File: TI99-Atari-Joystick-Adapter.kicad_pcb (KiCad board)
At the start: 2 copper layers, 13 parts, among them J1 DE9_Plug_MountingHoles, J2 DE9_Plug_MountingHoles, J3 DE9_Receptacle_MountingHoles

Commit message: Initial Design v0.01
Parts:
- added H1: MountingHole, MountingHole:MountingHole_2.5mm, F.Cu at (129.0, 59.0)
- added H2: MountingHole, MountingHole:MountingHole_2.5mm, F.Cu at (161.0, 59.0)
- added H3: MountingHole, MountingHole:MountingHole_2.5mm, F.Cu at (129.0, 132.0)
- added H4: MountingHole, MountingHole:MountingHole_2.5mm, F.Cu at (161.0, 132.0)
- D1, D10, D2, D3, D4, D5, D6, D7, D8, D9: value 1N4148W -> 1N4148
- moved J1 35.3 mm to (154.5, 84.4)
- moved J2 35.2 mm to (154.6, 117.7)
- moved J3 23.7 mm to (135.4, 100.7)
- moved D1 12.5 mm to (145.0, 80.0), turned to 180 degrees
- moved D10 1.12 mm to (145.0, 110.5), turned to 180 degrees
- moved D9 1.10 mm to (145.0, 107.1), turned to 180 degrees
- moved D8 1.09 mm to (145.0, 103.7), turned to 180 degrees
- moved D7 1.08 mm to (145.0, 100.3), turned to 180 degrees
- moved D6 1.07 mm to (145.0, 96.9), turned to 180 degrees
- moved D5 1.05 mm to (145.0, 93.5), turned to 180 degrees
- moved D4 1.04 mm to (145.0, 90.2), turned to 180 degrees
- moved D3 1.03 mm to (145.0, 86.8), turned to 180 degrees
- moved D2 1.03 mm to (145.0, 83.4), turned to 180 degrees
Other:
- board outline added: 40 x 81 mm
- board text added: "TI-99/4A - Atari Joystick Adapter"
- board text added: "https://github.com/jaymclain/TI99-Atari-Joystick-Adapter"
- board text added: "v0.01"

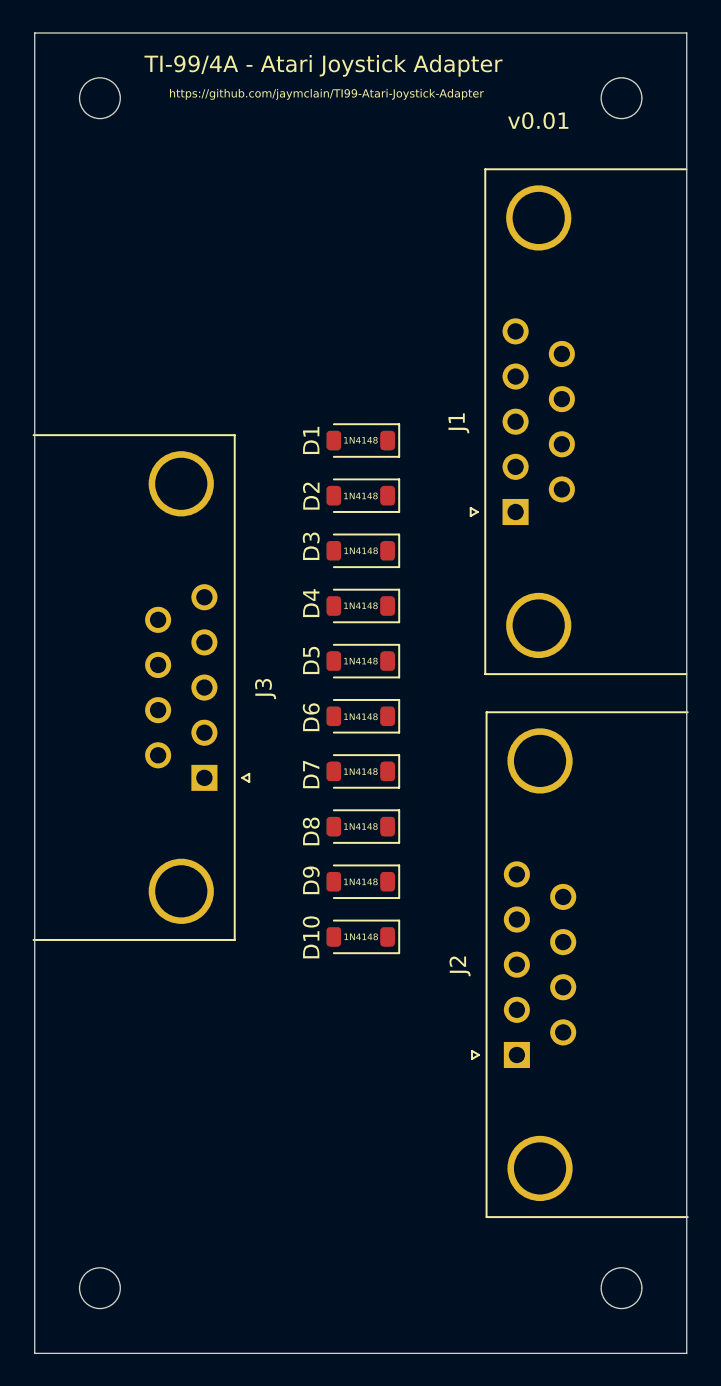
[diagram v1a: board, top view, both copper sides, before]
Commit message: Update board size, add tracks & vias and board image.
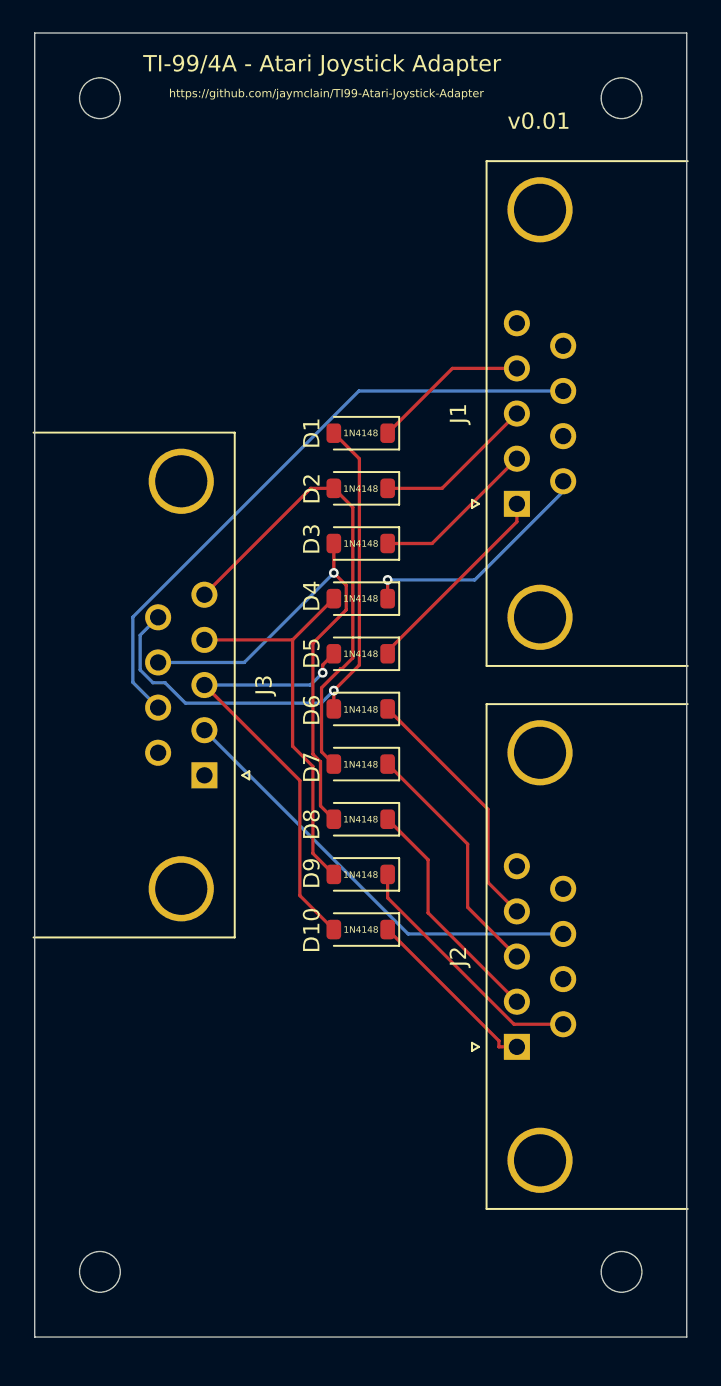
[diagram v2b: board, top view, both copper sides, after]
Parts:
- moved H3 1.00 mm to (129.0, 131.0)
- moved H4 1.00 mm to (161.0, 131.0)
- moved J1 0.51 mm to (154.6, 83.9)
- moved J2 0.50 mm to (154.6, 117.2)
- moved D1 0.45 mm to (145.0, 79.5)
- moved D10 0.45 mm to (145.0, 110.0)
- moved D2 0.45 mm to (145.0, 82.9)
- moved D3 0.45 mm to (145.0, 86.3)
- moved D4 0.45 mm to (145.0, 89.7)
- moved D5 0.45 mm to (145.0, 93.1)
- moved D6 0.45 mm to (145.0, 96.5)
- moved D7 0.45 mm to (145.0, 99.8)
- moved D8 0.45 mm to (145.0, 103.2)
- moved D9 0.45 mm to (145.0, 106.6)
- moved J3 0.15 mm to (135.4, 100.5)
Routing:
- net Net-(J1-Pad8): track 0.00 -> 38.3 mm
- net Net-(D1-A): track 0.00 -> 34.9 mm, vias 0 -> 1
- net Net-(D3-A): track 0.00 -> 31.7 mm, vias 0 -> 1
- net Net-(D2-A): track 0.00 -> 29.2 mm
- net Net-(D10-A): track 0.00 -> 27.3 mm, vias 0 -> 1
- net Net-(J2-Pad8): track 0.00 -> 27.2 mm
- net Net-(D4-A): track 0.00 -> 24.4 mm
- net Net-(D6-K): track 0.00 -> 15.7 mm
- net Net-(D9-K): track 0.00 -> 15.4 mm
- net Net-(D7-K): track 0.00 -> 15.1 mm
- net Net-(D4-K): track 0.00 -> 14.8 mm, vias 0 -> 1
- net Net-(D8-K): track 0.00 -> 14.5 mm
- net Net-(D5-K): track 0.00 -> 12.5 mm
- net Net-(D10-K): track 0.00 -> 11.1 mm
- net Net-(D3-K): track 0.00 -> 10.1 mm
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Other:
- board size 40 x 81 mm -> 40 x 80 mm
